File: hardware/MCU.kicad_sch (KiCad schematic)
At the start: 2 parts, among them U1 NUCLEO-L432KC, U2 SN65HVD230

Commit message: improve fuse connectios
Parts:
- removed U2: SN65HVD230, Package_SO:SOIC-8_3.9x4.9mm_P1.27mm, symbol Interface_CAN_LIN:SN65HVD230
- added U2: CAN_Transceiver, symbol wafel-eval-board:CAN_Transceiver_8Pin
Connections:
- net +5V: now also U2.3 (VCC)
- net GND: now also U2.2 (GND)
- net SPI.SCLK: now reaches U1.CN4_15 (PB3)
- net SPI.CS: now reaches U1.CN4_9 (PA4)
- net CAN_RX: now reaches U1.CN3_13 (PA11)
- net CAN_RX: now also U2.4 (RXD)
- net SPI.MOSI: now reaches U1.CN3_14 (PB5)
- net SPI.MISO: now reaches U1.CN3_15 (PB4)
- net CAN_TX: now reaches U1.CN3_5 (PA12)
- net CAN_TX: now also U2.1 (TXD)
- net CAN_STB: now reaches U1.CN3_6 (PB0)
- net CAN_STB: now also U2.8 (STB)
- new net +3.3V: U2.5 (VIO)
- new net CAN.H: U2.7 (CAN_H)
- new net CAN.L: U2.6 (CAN_L)
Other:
- moved on the sheet: U1A, U1B

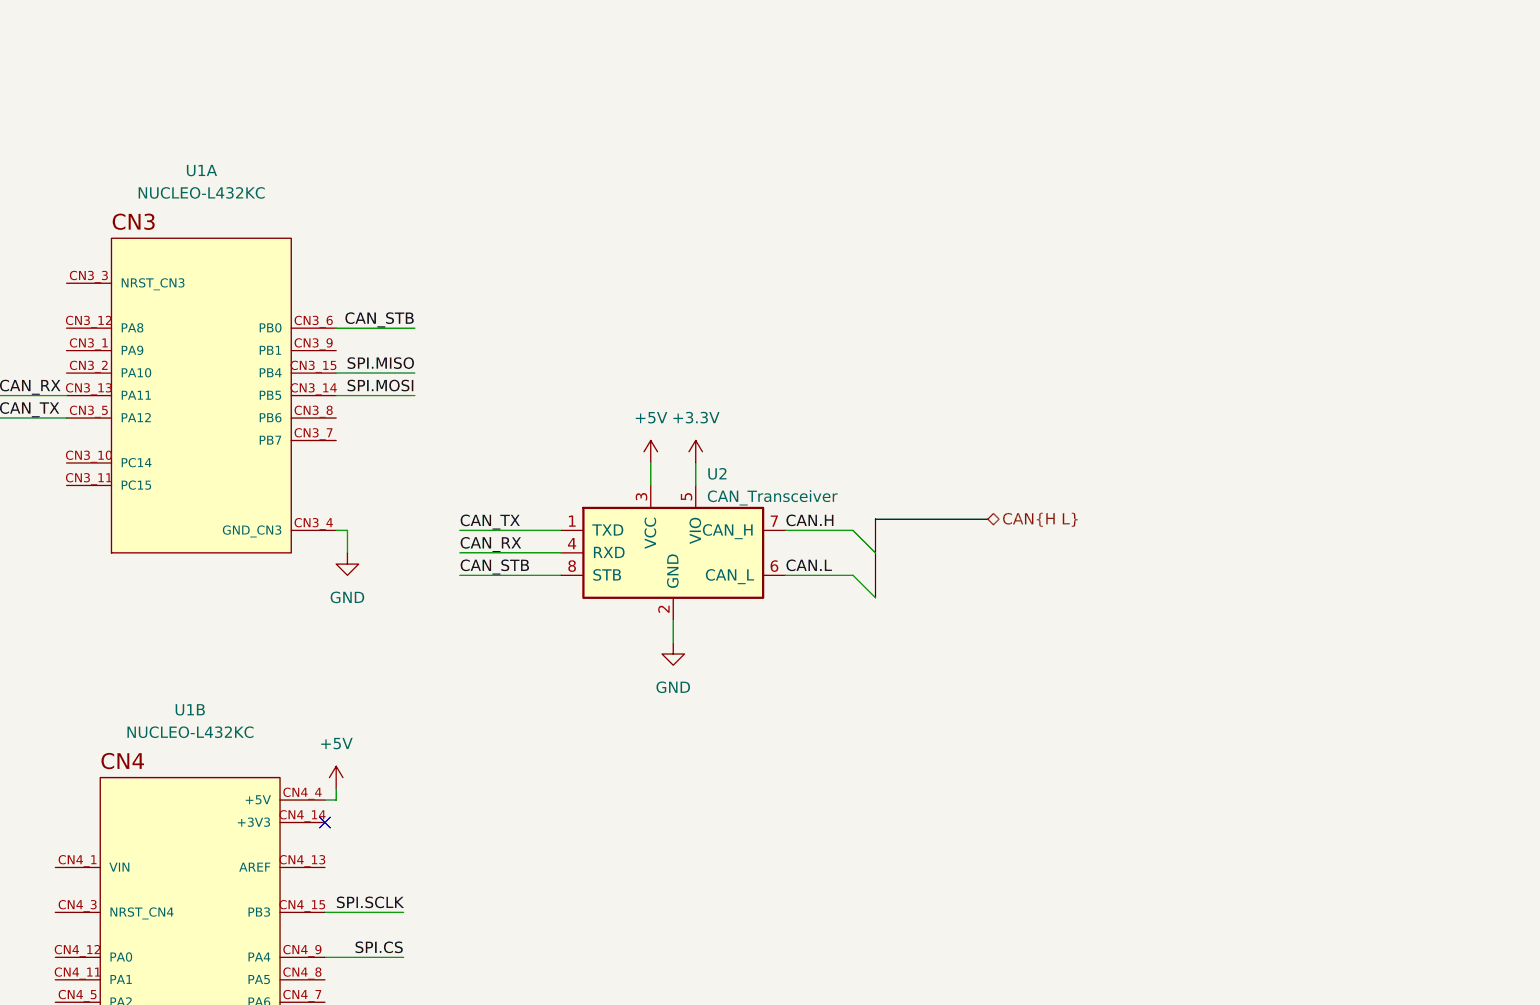
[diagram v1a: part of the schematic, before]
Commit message: remove jetbrains mcps, add uv in home and update flake
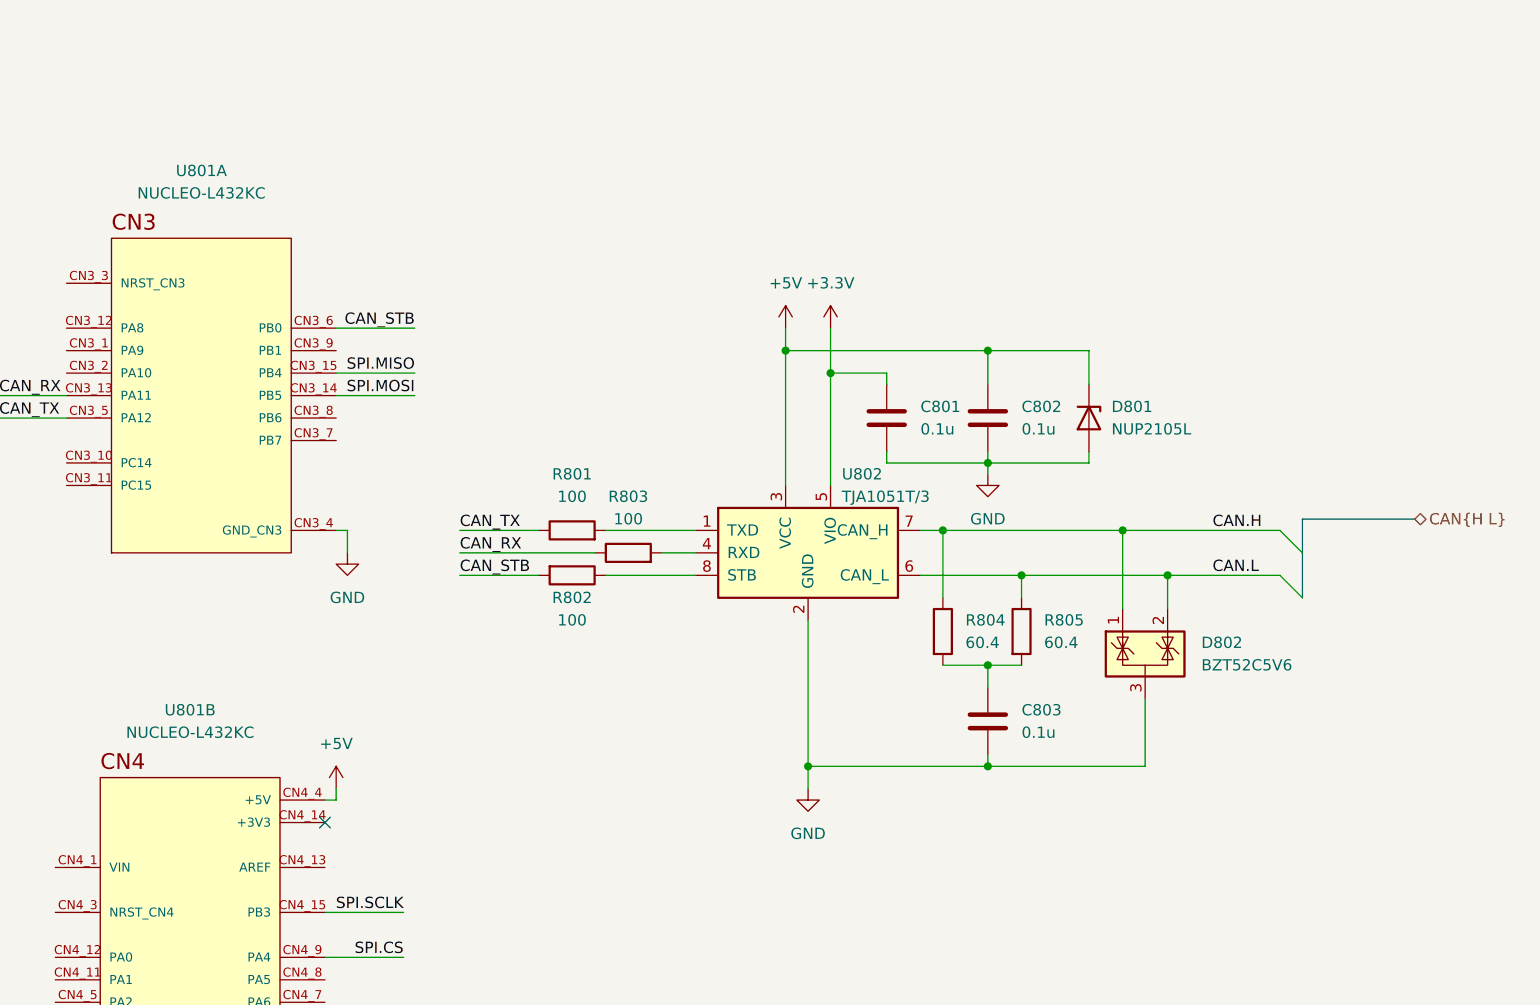
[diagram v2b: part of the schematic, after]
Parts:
- added C801, C802, C803: 0.1u, Capacitor_SMD:C_0603_1608Metric, symbol Device:C
- added D801: NUP2105L, Package_TO_SOT_SMD:SOT-23, symbol Device:D_Zener
- added D802: BZT52C5V6, Diode_SMD:D_SOD-123, symbol Power_Protection:SZNUP2105L
- added R801, R802, R803: 100, Resistor_SMD:R_0603_1608Metric, symbol Device:R
- added R804, R805: 60.4, Resistor_SMD:R_0603_1608Metric, symbol Device:R
- U802: renamed from U2; value CAN_Transceiver -> TJA1051T/3; footprint (none) -> Package_SO:SOIC-8_3.9x4.9mm_P1.27mm
- renumbered U1 to U801
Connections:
- net +3.3V: now also C801.1
- net +5V: now also C802.1, D801.1 (K)
- net CAN.H: now also D802.1 (K), R804.1
- net CAN.L: now also D802.2 (K), R805.1
- net CAN_RX: now also R803.1; no longer U802.4 (RXD)
- net CAN_STB: now also R802.2; no longer U802.8 (STB)
- net CAN_TX: now also R801.1; no longer U802.1 (TXD)
- net GND: now also C801.2, C802.2, C803.2, D801.2 (A), D802.3 (A)
- new net: R802.1, U802.8 (STB)
- new net: C803.1, R804.2, R805.2
- new net: R801.2, U802.1 (TXD)
- new net: R803.2, U802.4 (RXD)
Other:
- moved on the sheet: U802

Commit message: fixes
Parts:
- added C804: 470u, symbol Device:C
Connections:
- net GND: now also C804.2
- net BAT.ADC: now reaches U801.CN4_8 (PA5)
- net BAT.ADC: now also C804.1
- net BAT.EN: now reaches U801.CN3_9 (PB1)

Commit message: add bat{en adc}
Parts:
- renumbered C804 to C801, C801 to C802, C802 to C803, C803 to C804
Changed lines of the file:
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@@
 		(dnp no)
 		(fields_autoplaced yes)
-		(property "Reference" "#PWR0804"
+		(property "Reference" "#PWR0805"
 			(at 199.39 71.12 0)
 			(hide yes)
@@
 			(project "wafel-eval-board"
 				(path "/3e668e3e-3e16-4665-a807-4735962c41d3/95f215e1-2c63-4fc6-b759-568a8f71e3cc"
-					(reference "#PWR0804")
+					(reference "#PWR0805")
 					(unit 1)
 				)
@@
 		(dnp no)
 		(fields_autoplaced yes)
-		(property "Reference" "C803"
+		(property "Reference" "C804"
 			(at 226.06 110.4899 0)
 			(show_name no)
@@
 			(project "wafel-eval-board"
 				(path "/3e668e3e-3e16-4665-a807-4735962c41d3/95f215e1-2c63-4fc6-b759-568a8f71e3cc"
-					(reference "C803")
+					(reference "C804")
 					(unit 1)
 				)
@@
 		(dnp no)
 		(fields_autoplaced yes)
-		(property "Reference" "#PWR0808"
+		(property "Reference" "#PWR0804"
 			(at 161.29 160.02 0)
 			(hide yes)
@@
 			(project "wafel-eval-board"
 				(path "/3e668e3e-3e16-4665-a807-4735962c41d3/95f215e1-2c63-4fc6-b759-568a8f71e3cc"
-					(reference "#PWR0808")
+					(reference "#PWR0804")
 					(unit 1)
 				)
@@
 		(dnp no)
 		(fields_autoplaced yes)
-		(property "Reference" "C802"
+		(property "Reference" "C803"
 			(at 226.06 76.1999 0)
 			(show_name no)
@@
 			(project "wafel-eval-board"
 				(path "/3e668e3e-3e16-4665-a807-4735962c41d3/95f215e1-2c63-4fc6-b759-568a8f71e3cc"
-					(reference "C802")
+					(reference "C803")
 					(unit 1)
 				)
@@
 		(dnp no)
 		(fields_autoplaced yes)
-		(property "Reference" "#PWR0806"
+		(property "Reference" "#PWR0807"
 			(at 204.47 71.12 0)
 			(hide yes)
@@
 			(project "wafel-eval-board"
 				(path "/3e668e3e-3e16-4665-a807-4735962c41d3/95f215e1-2c63-4fc6-b759-568a8f71e3cc"
-					(reference "#PWR0806")
+					(reference "#PWR0807")
 					(unit 1)
 				)
@@
 		(dnp no)
 		(fields_autoplaced yes)
-		(property "Reference" "C801"
+		(property "Reference" "C802"
 			(at 214.63 76.1999 0)
 			(show_name no)
@@
 			(project "wafel-eval-board"
 				(path "/3e668e3e-3e16-4665-a807-4735962c41d3/95f215e1-2c63-4fc6-b759-568a8f71e3cc"
-					(reference "C801")
+					(reference "C802")
 					(unit 1)
 				)
@@
 		(dnp no)
 		(fields_autoplaced yes)
-		(property "Reference" "#PWR0807"
+		(property "Reference" "#PWR0808"
 			(at 222.25 90.17 0)
 			(hide yes)
@@
 			(project "wafel-eval-board"
 				(path "/3e668e3e-3e16-4665-a807-4735962c41d3/95f215e1-2c63-4fc6-b759-568a8f71e3cc"
-					(reference "#PWR0807")
+					(reference "#PWR0808")
 					(unit 1)
 				)
@@
 		(dnp no)
 		(fields_autoplaced yes)
-		(property "Reference" "C804"
+		(property "Reference" "C801"
 			(at 165.1 144.7799 0)
 			(show_name no)
@@
 			(project "wafel-eval-board"
 				(path "/3e668e3e-3e16-4665-a807-4735962c41d3/95f215e1-2c63-4fc6-b759-568a8f71e3cc"
-					(reference "C804")
+					(reference "C801")
 					(unit 1)
 				)
@@
 		(dnp no)
 		(fields_autoplaced yes)
-		(property "Reference" "#PWR0805"
+		(property "Reference" "#PWR0806"
 			(at 201.93 125.73 0)
 			(hide yes)
@@
 			(project "wafel-eval-board"
 				(path "/3e668e3e-3e16-4665-a807-4735962c41d3/95f215e1-2c63-4fc6-b759-568a8f71e3cc"
-					(reference "#PWR0805")
+					(reference "#PWR0806")
 					(unit 1)
 				)

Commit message: x
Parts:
- C801: footprint (none) -> Capacitor_SMD:C_0805_2012Metric
- C802, C803, C804: footprint Capacitor_SMD:C_0603_1608Metric -> Capacitor_SMD:C_0805_2012Metric
- R801, R802, R803, R804, R805: footprint Resistor_SMD:R_0603_1608Metric -> Resistor_SMD:R_0805_2012Metric
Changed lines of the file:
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@@
 			)
 		)
-		(property "Footprint" "Resistor_SMD:R_0603_1608Metric"
+		(property "Footprint" "Resistor_SMD:R_0805_2012Metric"
 			(at 175.26 93.472 90)
 			(hide yes)
@@
 			)
 		)
-		(property "Footprint" "Capacitor_SMD:C_0603_1608Metric"
+		(property "Footprint" "Capacitor_SMD:C_0805_2012Metric"
 			(at 223.2152 115.57 0)
 			(hide yes)
@@
 			)
 		)
-		(property "Footprint" "Capacitor_SMD:C_0603_1608Metric"
+		(property "Footprint" "Capacitor_SMD:C_0805_2012Metric"
 			(at 223.2152 81.28 0)
 			(hide yes)
@@
 			)
 		)
-		(property "Footprint" "Resistor_SMD:R_0603_1608Metric"
+		(property "Footprint" "Resistor_SMD:R_0805_2012Metric"
 			(at 175.26 91.948 90)
 			(hide yes)
@@
 			)
 		)
-		(property "Footprint" "Capacitor_SMD:C_0603_1608Metric"
+		(property "Footprint" "Capacitor_SMD:C_0805_2012Metric"
 			(at 211.7852 81.28 0)
 			(hide yes)
@@
 			)
 		)
-		(property "Footprint" "Resistor_SMD:R_0603_1608Metric"
+		(property "Footprint" "Resistor_SMD:R_0805_2012Metric"
 			(at 181.61 94.488 90)
 			(hide yes)
@@
 			)
 		)
-		(property "Footprint" "Resistor_SMD:R_0603_1608Metric"
+		(property "Footprint" "Resistor_SMD:R_0805_2012Metric"
 			(at 215.392 101.6 90)
 			(hide yes)
@@
 			)
 		)
-		(property "Footprint" ""
+		(property "Footprint" "Capacitor_SMD:C_0805_2012Metric"
 			(at 162.2552 149.86 0)
 			(hide yes)
@@
 			)
 		)
-		(property "Footprint" "Resistor_SMD:R_0603_1608Metric"
+		(property "Footprint" "Resistor_SMD:R_0805_2012Metric"
 			(at 224.282 101.6 90)
 			(hide yes)

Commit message: x
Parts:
- added R806: 100, Resistor_SMD:R_0805_2012Metric, symbol Device:R
- added U803: PC817, symbol Isolator:Optocoupler_DC_PhotoNPN_AKEC
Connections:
- net GND: now also R806.2
- net VESC_SW: now reaches U801.CN3_8 (PB6)
- net VESC_SW: now also U803.1
- new net: R806.1, U803.2
- new net VESC.GND: U803.3
- new net VESC.SW: U803.4

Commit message: x
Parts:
- added F802: 0.2A, Fuse:Fuse_Littelfuse-NANO2-451_453, symbol Device:Fuse
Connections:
- net +5V: now also F802.2; no longer C803.1, D801.1 (K), U801.CN4_4 (+5V), U802.3 (VCC)
- new net: C803.1, D801.1 (K), F802.1, U802.3 (VCC)
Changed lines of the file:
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@@
 	)
 	(no_connect
-		(at 147.32 123.19)
+		(at 147.32 120.65)
 	)
 	(bus_entry
@@
 	(wire
 		(pts
+			(xy 149.86 111.76) (xy 149.86 113.03)
+		)
+		(stroke
+			(width 0)
+			(type default)
+		)
+	)
+	(wire
+		(pts
 			(xy 240.03 116.84) (xy 222.25 116.84)
 		)
@@
 	(wire
 		(pts
-			(xy 204.47 67.31) (xy 204.47 72.39)
+			(xy 204.47 59.69) (xy 204.47 72.39)
 		)
 		(stroke
@@
 	(wire
 		(pts
+			(xy 147.32 123.19) (xy 149.86 123.19)
+		)
+		(stroke
+			(width 0)
+			(type default)
+		)
+	)
+	(wire
+		(pts
 			(xy 162.56 95.25) (xy 171.45 95.25)
 		)
@@
 	(wire
 		(pts
+			(xy 199.39 68.58) (xy 199.39 69.85)
+		)
+		(stroke
+			(width 0)
+			(type default)
+		)
+	)
+	(wire
+		(pts
 			(xy 110.49 74.93) (xy 118.11 74.93)
 		)
@@
 	(wire
 		(pts
+			(xy 199.39 59.69) (xy 199.39 60.96)
+		)
+		(stroke
+			(width 0)
+			(type default)
+		)
+	)
+	(wire
+		(pts
 			(xy 161.29 149.86) (xy 161.29 153.67)
 		)
@@
 	(wire
 		(pts
-			(xy 148.59 120.65) (xy 147.32 120.65)
-		)
-		(stroke
-			(width 0)
-			(type default)
-		)
-	)
-	(wire
-		(pts
 			(xy 217.17 105.41) (xy 222.25 105.41)
 		)
@@
 		)
 	)
+	(wire
+		(pts
+			(xy 149.86 123.19) (xy 149.86 120.65)
+		)
+		(stroke
+			(width 0)
+			(type default)
+		)
+	)
 	(bus
 		(pts
@@
 	(wire
 		(pts
-			(xy 199.39 67.31) (xy 199.39 69.85)
-		)
-		(stroke
-			(width 0)
-			(type default)
-		)
-	)
-	(wire
-		(pts
 			(xy 86.36 80.01) (xy 96.52 80.01)
 		)
@@
 		(pts
 			(xy 199.39 69.85) (xy 199.39 85.09)
-		)
-		(stroke
-			(width 0)
-			(type default)
-		)
-	)
-	(wire
-		(pts
-			(xy 148.59 119.38) (xy 148.59 120.65)
 		)
 		(stroke
@@
 	)
 	(symbol
-		(lib_id "power:+5V")
-		(at 148.59 119.38 0)
-		(unit 1)
-		(body_style 1)
-		(exclude_from_sim no)
-		(in_bom yes)
-		(on_board yes)
-		(in_pos_files yes)
-		(dnp no)
-		(fields_autoplaced yes)
-		(property "Reference" "#PWR0801"
-			(at 148.59 123.19 0)
-			(hide yes)
-			(show_name no)
-			(do_not_autoplace no)
-			(effects
-				(font
-					(size 1.27 1.27)
-				)
-			)
-		)
-		(property "Value" "+5V"
-			(at 148.59 114.3 0)
-			(show_name no)
-			(do_not_autoplace no)
-			(effects
-				(font
-					(size 1.27 1.27)
-				)
-			)
-		)
-		(property "Footprint" ""
-			(at 148.59 119.38 0)
-			(hide yes)
-			(show_name no)
-			(do_not_autoplace no)
-			(effects
-				(font
-					(size 1.27 1.27)
-				)
-			)
-		)
-		(property "Datasheet" ""
-			(at 148.59 119.38 0)
-			(hide yes)
-			(show_name no)
-			(do_not_autoplace no)
-			(effects
-				(font
-					(size 1.27 1.27)
-				)
-			)
-		)
-		(property "Description" "Power symbol creates a global label with name \"+5V\""
-			(at 148.59 119.38 0)
-			(hide yes)
-			(show_name no)
-			(do_not_autoplace no)
-			(effects
-				(font
-					(size 1.27 1.27)
-				)
-			)
-		)
-		(pin "1"
-		)
-		(instances
-			(project "wafel-eval-board"
-				(path "/3e668e3e-3e16-4665-a807-4735962c41d3/95f215e1-2c63-4fc6-b759-568a8f71e3cc"
-					(reference "#PWR0801")
-					(unit 1)
-				)
-			)
-		)
-	)
-	(symbol
 		(lib_id "Device:R")
 		(at 194.31 142.24 270)
@@
 	(symbol
 		(lib_id "power:+5V")
-		(at 199.39 67.31 0)
+		(at 199.39 59.69 0)
 		(unit 1)
 		(body_style 1)
@@
 		(fields_autoplaced yes)
 		(property "Reference" "#PWR0805"
-			(at 199.39 71.12 0)
+			(at 199.39 63.5 0)
 			(hide yes)
 			(show_name no)
@@
 		)
 		(property "Value" "+5V"
-			(at 199.39 62.23 0)
+			(at 199.39 54.61 0)
 			(show_name no)
 			(do_not_autoplace no)
@@
 		)
 		(property "Footprint" ""
-			(at 199.39 67.31 0)
+			(at 199.39 59.69 0)
 			(hide yes)
 			(show_name no)
@@
 		)
 		(property "Datasheet" ""
-			(at 199.39 67.31 0)
+			(at 199.39 59.69 0)
 			(hide yes)
 			(show_name no)
@@
 		)
 		(property "Description" "Power symbol creates a global label with name \"+5V\""
-			(at 199.39 67.31 0)
+			(at 199.39 59.69 0)
 			(hide yes)
 			(show_name no)
@@
 	(symbol
 		(lib_id "power:+3.3V")
-		(at 204.47 67.31 0)
+		(at 149.86 111.76 0)
+		(unit 1)
+		(body_style 1)
+		(exclude_from_sim no)
+		(in_bom yes)
+		(on_board yes)
+		(in_pos_files yes)
+		(dnp no)
+		(fields_autoplaced yes)
+		(property "Reference" "#PWR0801"
+			(at 149.86 115.57 0)
+			(hide yes)
+			(show_name no)
+			(do_not_autoplace no)
+			(effects
+				(font
+					(size 1.27 1.27)
+				)
+			)
+		)
+		(property "Value" "+3.3V"
+			(at 149.86 106.68 0)
+			(show_name no)
+			(do_not_autoplace no)
+			(effects
+				(font
+					(size 1.27 1.27)
+				)
+			)
+		)
+		(property "Footprint" ""
+			(at 149.86 111.76 0)
+			(hide yes)
+			(show_name no)
+			(do_not_autoplace no)
+			(effects
+				(font
+					(size 1.27 1.27)
+				)
+			)
+		)
+		(property "Datasheet" ""
+			(at 149.86 111.76 0)
+			(hide yes)
+			(show_name no)
+			(do_not_autoplace no)
+			(effects
+				(font
+					(size 1.27 1.27)
+				)
+			)
+		)
+		(property "Description" "Power symbol creates a global label with name \"+3.3V\""
+			(at 149.86 111.76 0)
+			(hide yes)
+			(show_name no)
+			(do_not_autoplace no)
+			(effects
+				(font
+					(size 1.27 1.27)
+				)
+			)
+		)
+		(pin "1"
+		)
+		(instances
+			(project "wafel-eval-board"
+				(path "/3e668e3e-3e16-4665-a807-4735962c41d3/95f215e1-2c63-4fc6-b759-568a8f71e3cc"
+					(reference "#PWR0801")
+					(unit 1)
+				)
+			)
+		)
+	)
+	(symbol
+		(lib_id "Device:Fuse")
+		(at 199.39 64.77 0)
+		(mirror x)
+		(unit 1)
+		(body_style 1)
+		(exclude_from_sim no)
+		(in_bom yes)
+		(on_board yes)
+		(in_pos_files yes)
+		(dnp no)
+		(property "Reference" "F802"
+			(at 195.58 63.5 0)
+			(show_name no)
+			(do_not_autoplace no)
+			(effects
+				(font
+					(size 1.27 1.27)
+				)
+			)
+		)
+		(property "Value" "0.2A"
+			(at 195.58 66.04 0)
+			(show_name no)
+			(do_not_autoplace no)
+			(effects
+				(font
+					(size 1.27 1.27)
+				)
+			)
+		)
+		(property "Footprint" "Fuse:Fuse_Littelfuse-NANO2-451_453"
+			(at 197.612 64.77 90)
+			(hide yes)
+			(show_name no)
+			(do_not_autoplace no)
+			(effects
+				(font
+					(size 1.27 1.27)
+				)
+			)
+		)
+		(property "Datasheet" ""
+			(at 199.39 64.77 0)
+			(hide yes)
+			(show_name no)
+			(do_not_autoplace no)
+			(effects
+				(font
+					(size 1.27 1.27)
+				)
+			)
+		)
+		(property "Description" "Fuse"
+			(at 199.39 64.77 0)
+			(hide yes)
+			(show_name no)
+			(do_not_autoplace no)
+			(effects
+				(font
+					(size 1.27 1.27)
+				)
+			)
+		)
+		(property "LCSC" "C178980"
+			(at 199.39 64.77 90)
+			(hide yes)
+			(show_name no)
+			(do_not_autoplace no)
+			(effects
+				(font
+					(size 1.27 1.27)
+				)
+			)
+		)
+		(pin "2"
+		)
+		(pin "1"
+		)
+		(instances
+			(project "wafel-eval-board"
+				(path "/3e668e3e-3e16-4665-a807-4735962c41d3/95f215e1-2c63-4fc6-b759-568a8f71e3cc"
+					(reference "F802")
+					(unit 1)
+				)
+			)
+		)
+	)
+	(symbol
+		(lib_id "power:+3.3V")
+		(at 204.47 59.69 0)
 		(unit 1)
 		(body_style 1)
@@
 		(fields_autoplaced yes)
 		(property "Reference" "#PWR0807"
-			(at 204.47 71.12 0)
+			(at 204.47 63.5 0)
 			(hide yes)
 			(show_name no)
@@
 		)
 		(property "Value" "+3.3V"
-			(at 204.47 62.23 0)
+			(at 204.47 54.61 0)
 			(show_name no)
 			(do_not_autoplace no)
@@
 		)
 		(property "Footprint" ""
-			(at 204.47 67.31 0)
+			(at 204.47 59.69 0)
 			(hide yes)
 			(show_name no)
@@
 		)
 		(property "Datasheet" ""
-			(at 204.47 67.31 0)
+			(at 204.47 59.69 0)
 			(hide yes)
 			(show_name no)
@@
 		)
 		(property "Description" "Power symbol creates a global label with name \"+3.3V\""
-			(at 204.47 67.31 0)
-			(hide yes)
-			(show_name no)
+			(at 204.47 59.69 0)
+			(hide yes)
+			(show_name no)
